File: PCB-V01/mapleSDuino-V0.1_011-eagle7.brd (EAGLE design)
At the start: 79 x 27 mm, 12 parts, among them IC2 LAN-USR-ES1

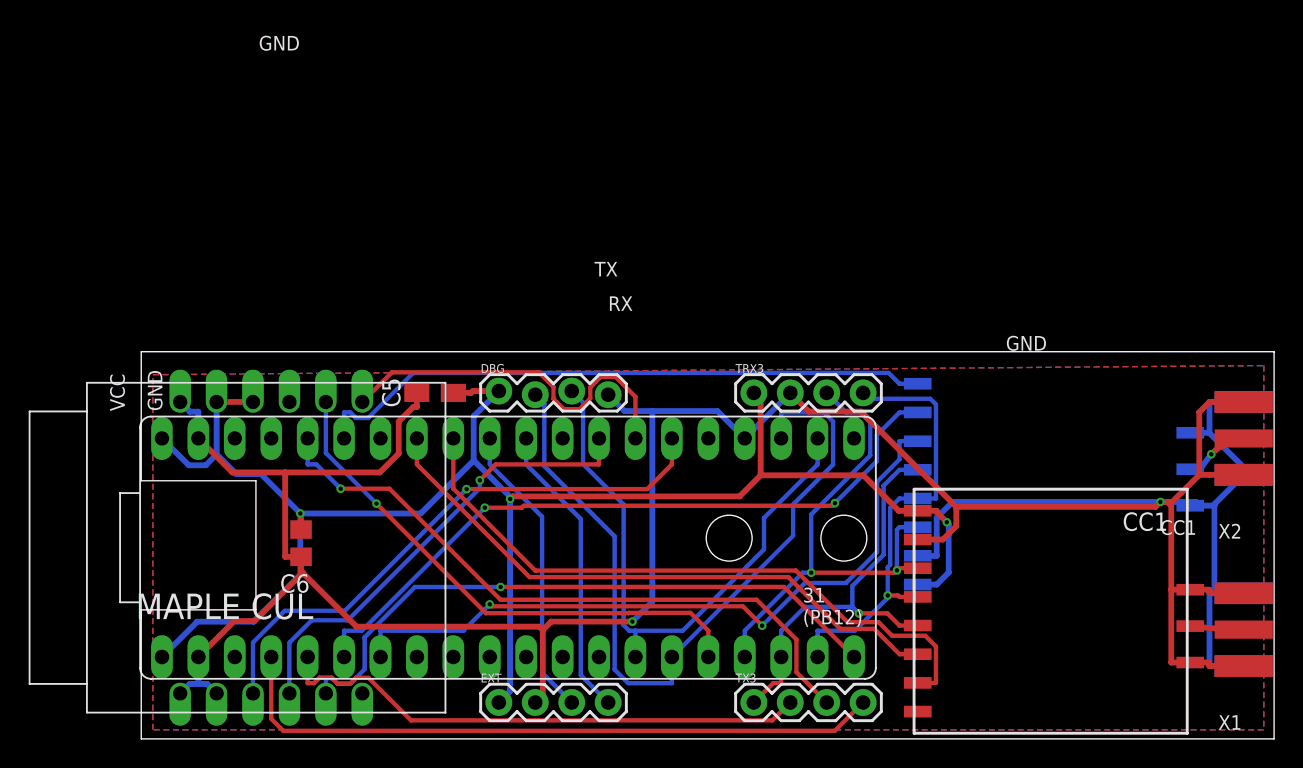
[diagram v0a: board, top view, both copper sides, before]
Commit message: Update
SPI + TRX Pins, Shielding, 5V Pin
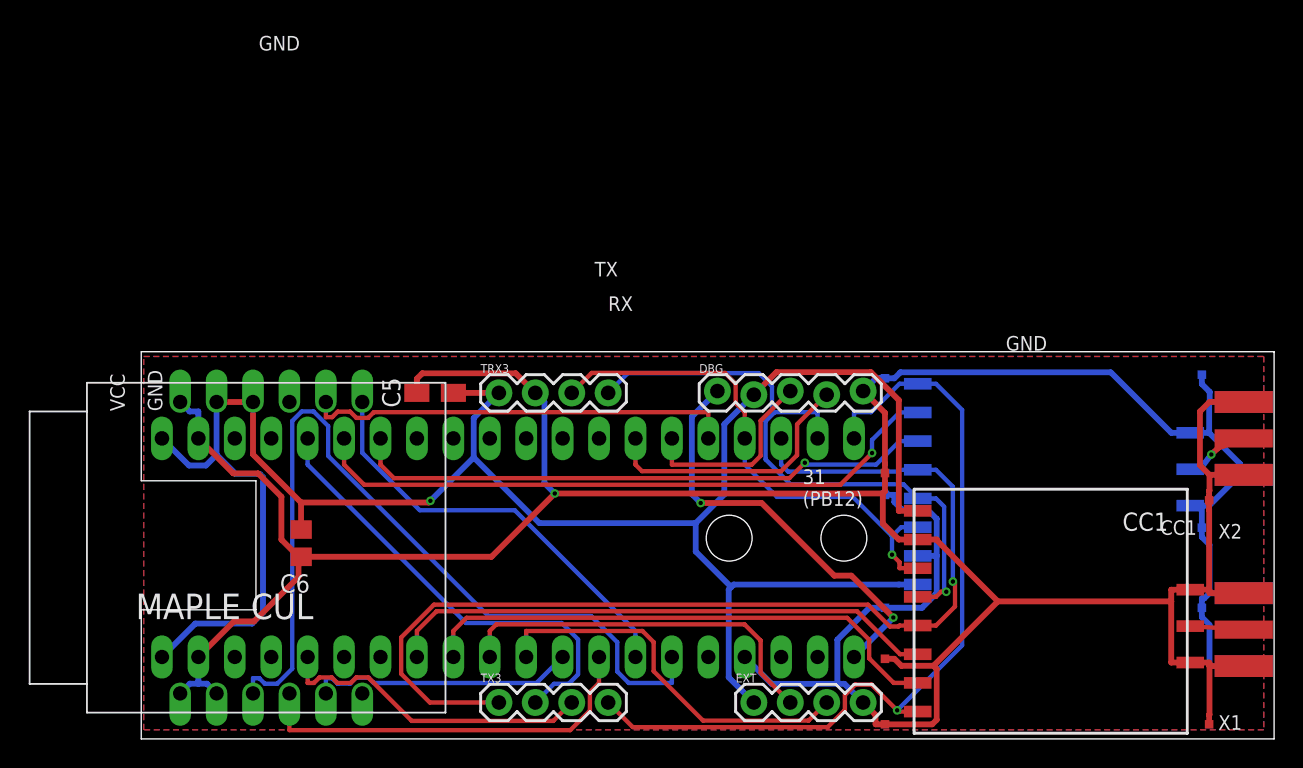
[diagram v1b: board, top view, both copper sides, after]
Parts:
- added TP1, TP10, TP11, TP2, TP3, TP4, TP5, TP6, TP7, TP8, TP9: TPTP06SQ, testpad:TP06SQ
- DBG: device SparkFun-Connectors:1X04_LOCK -> SparkFun-Connectors:1X05_LOCK
- moved EXT 17.8 mm to (45.7, 2.54)
- moved TRX3 17.8 mm to (27.9, 24.1)
- moved TX3 17.8 mm to (27.9, 2.54)
- moved DBG 15.2 mm to (43.2, 24.1)
- flipped U$1 to the bottom, turned to 180 degrees
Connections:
- removed net CC_CS0: CC1.CSN
- new net RX3: U$1.22
- new net TX3: U$1.23
- net +5V: now also DBG.1
- net CC_CS1: no longer CC2.CSN
- net CC_CS2: no longer TX3.4
- net GND: now also DBG.5, EXT.4, TP1.TP, TP10.TP, TP11.TP, TP2.TP, TP3.TP, TP4.TP, TP5.TP, TP6.TP, TP7.TP, TP8.TP, TP9.TP; no longer DBG.4, EXT.2
- net RX1: now also DBG.4; no longer DBG.3, U$1.22
- net RX2: now also EXT.3; no longer EXT.4
- net SS1: now also IC2.5
- net SS2: now also CC1.CSN, CC2.CSN, TX3.4; no longer IC2.5
- net TX1: now also DBG.3; no longer DBG.2, U$1.23
- net TX2: now also EXT.2; no longer EXT.3
- net VCC: now also DBG.2; no longer DBG.1
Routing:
- net CC_CS2: track 46.8 -> 0.00 mm
- net MISO2: track 29.1 -> 73.9 mm
- net CC_CS1: track 43.6 -> 0.00 mm
- net GND: track 230.5 -> 272.2 mm, vias 2 -> 1
- net TX1: track 54.4 -> 13.6 mm
- net +5V: track 0.00 -> 29.4 mm, vias 0 -> 2
- net CC_OUT_2: track 46.2 -> 22.5 mm, vias 1 -> 0
- net RX1: track 41.2 -> 18.8 mm
- net MOSI1: track 39.7 -> 60.5 mm, vias 1 -> 0
- net VCC: track 121.3 -> 140.9 mm, vias 3 -> 1
- net SS1: track 0.00 -> 18.8 mm
- net SS2: track 44.2 -> 58.7 mm
- net SCK2: track 31.6 -> 44.6 mm
- net CC_IN_1: track 49.6 -> 40.9 mm, vias 2 -> 1
- net CC_OUT_0: track 45.5 -> 37.2 mm
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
